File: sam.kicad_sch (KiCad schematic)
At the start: 70 parts, among them IC4 74ACT02, IC5 74ACT138, IC6 74ACT138N, J1 JTAG, J3 Conn_01x24, J4 Conn_01x24, U3 SN105125DBVR, U4 XC6SLX9-3TQG144I, U5 SN105125DBVR, X1 14.31818MHz

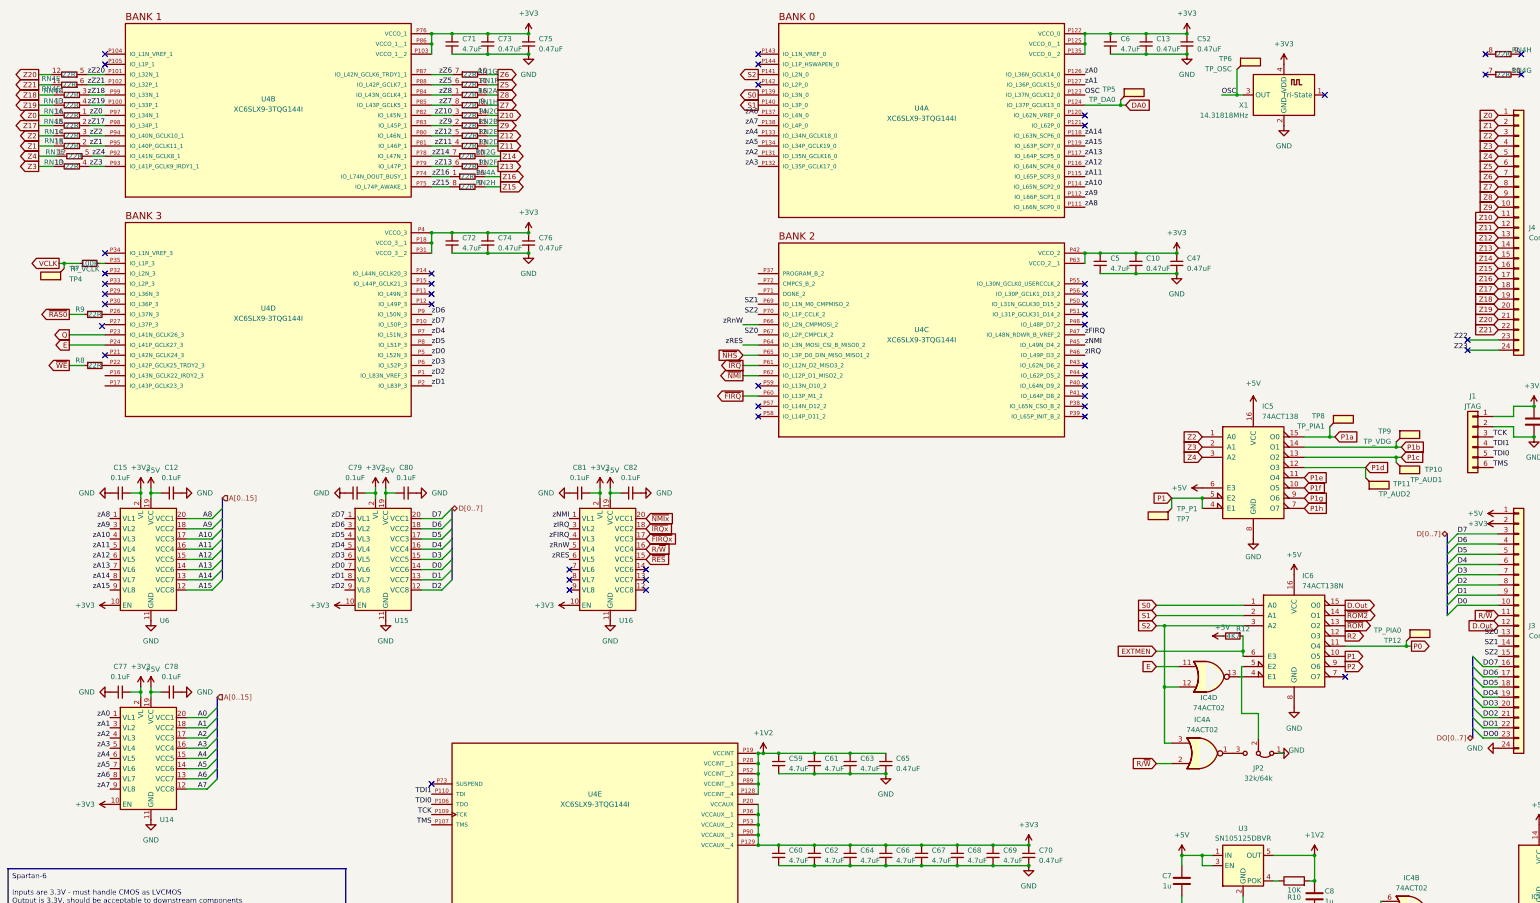
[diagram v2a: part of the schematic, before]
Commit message: add slot identification
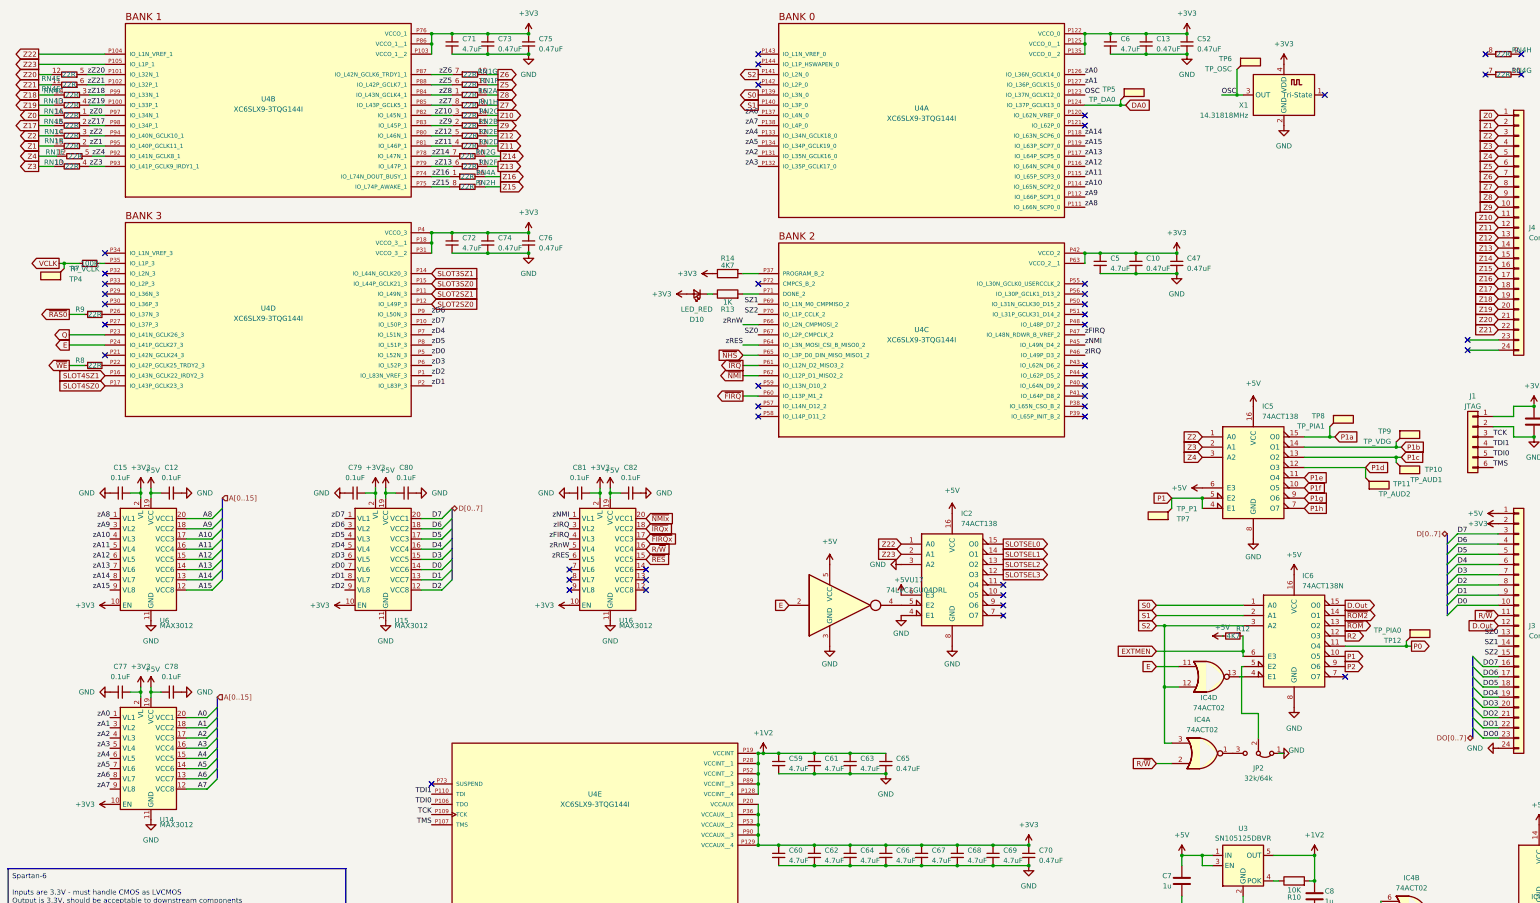
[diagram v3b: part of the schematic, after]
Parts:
- added D10: LED_RED, LED_SMD:LED_0805_2012Metric, symbol Device:LED_Small
- added IC2: 74ACT138, Package_SO:SOIC-16W_7.5x10.3mm_P1.27mm, symbol 74xx:74LS138
- added R13: 1K, Resistor_SMD:R_0805_2012Metric_Pad1.20x1.40mm_HandSolder, symbol Device:R
- added R14: 4K7, Resistor_SMD:R_0805_2012Metric_Pad1.20x1.40mm_HandSolder, symbol Device:R
- added U17: 74LVC1GU04DRL, Package_TO_SOT_SMD:SOT-553, symbol 74xGxx:74LVC1GU04DRL
- U14, U15, U16, U6: value ~ -> MAX3012; DigiKey (none) -> MAX3012EUP+-ND
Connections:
- net +3V3: now also D10.2 (A), R14.1
- net +5V: now also IC2.16 (VCC), IC2.6 (E3), U17.5 (VCC)
- net E: now also U17.2
- net GND: now also IC2.3 (A2), IC2.4 (E1), IC2.8 (GND), U17.3 (GND)
- net Z22: now also U4.P104 (IO_L1N_VREF_1), IC2.1 (A0); no longer J4.23 (Pin_23)
- net Z23: now also U4.P105 (IO_L1P_1), IC2.2 (A1); no longer J4.24 (Pin_24)
- net SLOT2SZ1: now reaches U4.P11 (IO_L49N_3)
- net SLOT2SZ0: now reaches U4.P12 (IO_L49P_3)
- net SLOT3SZ1: now reaches U4.P14 (IO_L44N_GCLK20_3)
- net SLOT3SZ0: now reaches U4.P15 (IO_L44P_GCLK21_3)
- net SLOT4SZ1: now reaches U4.P16 (IO_L43N_GCLK22_IRDY2_3)
- net SLOT4SZ0: now reaches U4.P17 (IO_L43P_GCLK23_3)
- net at U3.4 (POK): now also R10.1
- net at U4.P37 (PROGRAM_B_2): now also R14.2
- net at U4.P71 (DONE_2): now also R13.2
- new net: IC2.5 (E2), U17.4
- new net: D10.1 (K), R13.1
- new net SLOTSEL0: IC2.15 (O0)
- new net SLOTSEL1: IC2.14 (O1)
- new net SLOTSEL2: IC2.13 (O2)
- new net SLOTSEL3: IC2.12 (O3)
- no-connect marks 47 -> 46

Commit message: add data bus transceiver
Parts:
- added C83: 0.01uF, Capacitor_SMD:C_0805_2012Metric_Pad1.18x1.45mm_HandSolder, symbol Device:C_Small
- added U19: 74ACT245, Package_SO:TSSOP-20_4.4x5mm_P0.5mm, symbol 74xx:74LS245
- C10, C13, C47, C52, C65, C70, C73, C74, C75, C76: DigiKey (none) -> 399-C0805C474K4RAC7800CT-ND
- C11, C8: DigiKey (none) -> 399-C0805C105K4RAC7800CT-ND; LCSC Part C961513 -> (none)
- C12, C15, C77, C78, C79, C80, C81, C82: DigiKey (none) -> 399-C0805C104K4RAC7800CT-ND
- C14: value 100n -> 0.1uF; DigiKey (none) -> 399-C0805C104K4RAC7800CT-ND; JLCPCB BOM 0 -> (none); LCSC Part C149620 -> (none)
- C5, C59, C6, C60, C61, C62, C63, C64, C66, C67, C68, C69, C71, C72: DigiKey (none) -> 399-C0805C475K4RAC7800CT-ND
- C7, C9: DigiKey (none) -> 399-C0805C105K4RAC7800CT-ND; LCSC Part C77080 -> (none)
- D10: DigiKey (none) -> 67-SML-LXF0805SRD-TRCT-ND
- R10, R11: DigiKey (none) -> RNCP0805FTD10K0CT-ND
- R12: DigiKey CF14JT4K70CT-ND -> 541-4131-1-ND
- R13: DigiKey (none) -> RNCP0805FTD1K00CT-ND
- R14: DigiKey (none) -> 541-4131-1-ND
- R7: DigiKey CF14JT22R0CT-ND -> RNCP0805FTD100RCT-ND
- R8, R9: DigiKey CF14JT22R0CT-ND -> RPC0805JT22R0CT-ND
- U17: DigiKey (none) -> 296-18657-1-ND
- U4: value XC6SLX9-3TQG144I -> XC6SLX9-2TQG144I; Check_prices https://www.snapeda.com/parts/XC6SLX9-3TQG144I/Xilinx+Inc./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 -> (none); DigiKey (none) -> 122-1748-ND; DigiKey_Part_Number 122-1748-ND -> (none); MANUFACTURER Xilinx Inc. -> (none); MF Xilinx Inc. -> (none); MP XC6SLX9-3TQG144I -> (none); PARTREV 3.1.1 -> (none); Package TQFP-144 Xilinx -> (none); Purchase-URL https://www.snapeda.com/api/url_track_click_mouser/?unipart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 -> (none); STANDARD IPC-7351B -> (none); SnapEDA_Link https://www.snapeda.com/parts/XC6SLX9-3TQG144I/Xilinx+Inc./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 -> (none)
- X1: DigiKey (none) -> XC1405CT-ND; LCSC Part C5119017 -> (none); RS https://uk.rs-online.com/web/p/crystal-oscillators/1721882 -> (none)
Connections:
- net +3V3: now also X1.1 (Tri-State), C83.1
- net +5V: now also U19.20 (VCC)
- net D0: now also U19.9 (A7)
- net D1: now also U19.8 (A6)
- net D2: now also U19.7 (A5)
- net D3: now also U19.6 (A4)
- net D4: now also U19.5 (A3)
- net D5: now also U19.4 (A2)
- net D6: now also U19.3 (A1)
- net D7: now also U19.2 (A0)
- net GND: now also C83.2, U19.10 (GND)
- net Z22: now also J4.23 (Pin_23), RN4.10; no longer U4.P104 (IO_L1N_VREF_1)
- net Z23: now also J4.24 (Pin_24), RN4.9; no longer U4.P105 (IO_L1P_1)
- net at U3.4 (POK): now also R10.1
- net CPU_DIR: now reaches U4.P43 (IO_L62N_D6_2)
- net CPU_DIR: now also U19.1 (A->B)
- net ~{CPU_DATA}: now reaches U4.P44 (IO_L62P_D5_2)
- net ~{CPU_DATA}: now also U19.19 (CE)
- net zZ23: now reaches RN4.8
- net zZ23: now also U4.P105 (IO_L1P_1)
- net zZ22: now reaches RN4.7
- net zZ22: now also U4.P104 (IO_L1N_VREF_1)
- new net DC0: U19.11 (B7)
- new net DC1: U19.12 (B6)
- new net DC2: U19.13 (B5)
- new net DC3: U19.14 (B4)
- new net DC4: U19.15 (B3)
- new net DC5: U19.16 (B2)
- new net DC6: U19.17 (B1)
- new net DC7: U19.18 (B0)
- no-connect marks 46 -> 37
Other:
- moved on the sheet: RN4G, RN4H
